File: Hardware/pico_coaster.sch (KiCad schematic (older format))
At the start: 143 parts, among them J1 Conn_02x06_Odd_Even, J2 Conn_02x06_Odd_Even, J3 Conn_02x06_Odd_Even, J4 Conn_01x04, J5 USB_C_Receptacle_USB2.0, SW1 SW_Push, SW2 SW_Push, SW3 SW_Push, SW4 SW_Push, SW5 SW_Push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

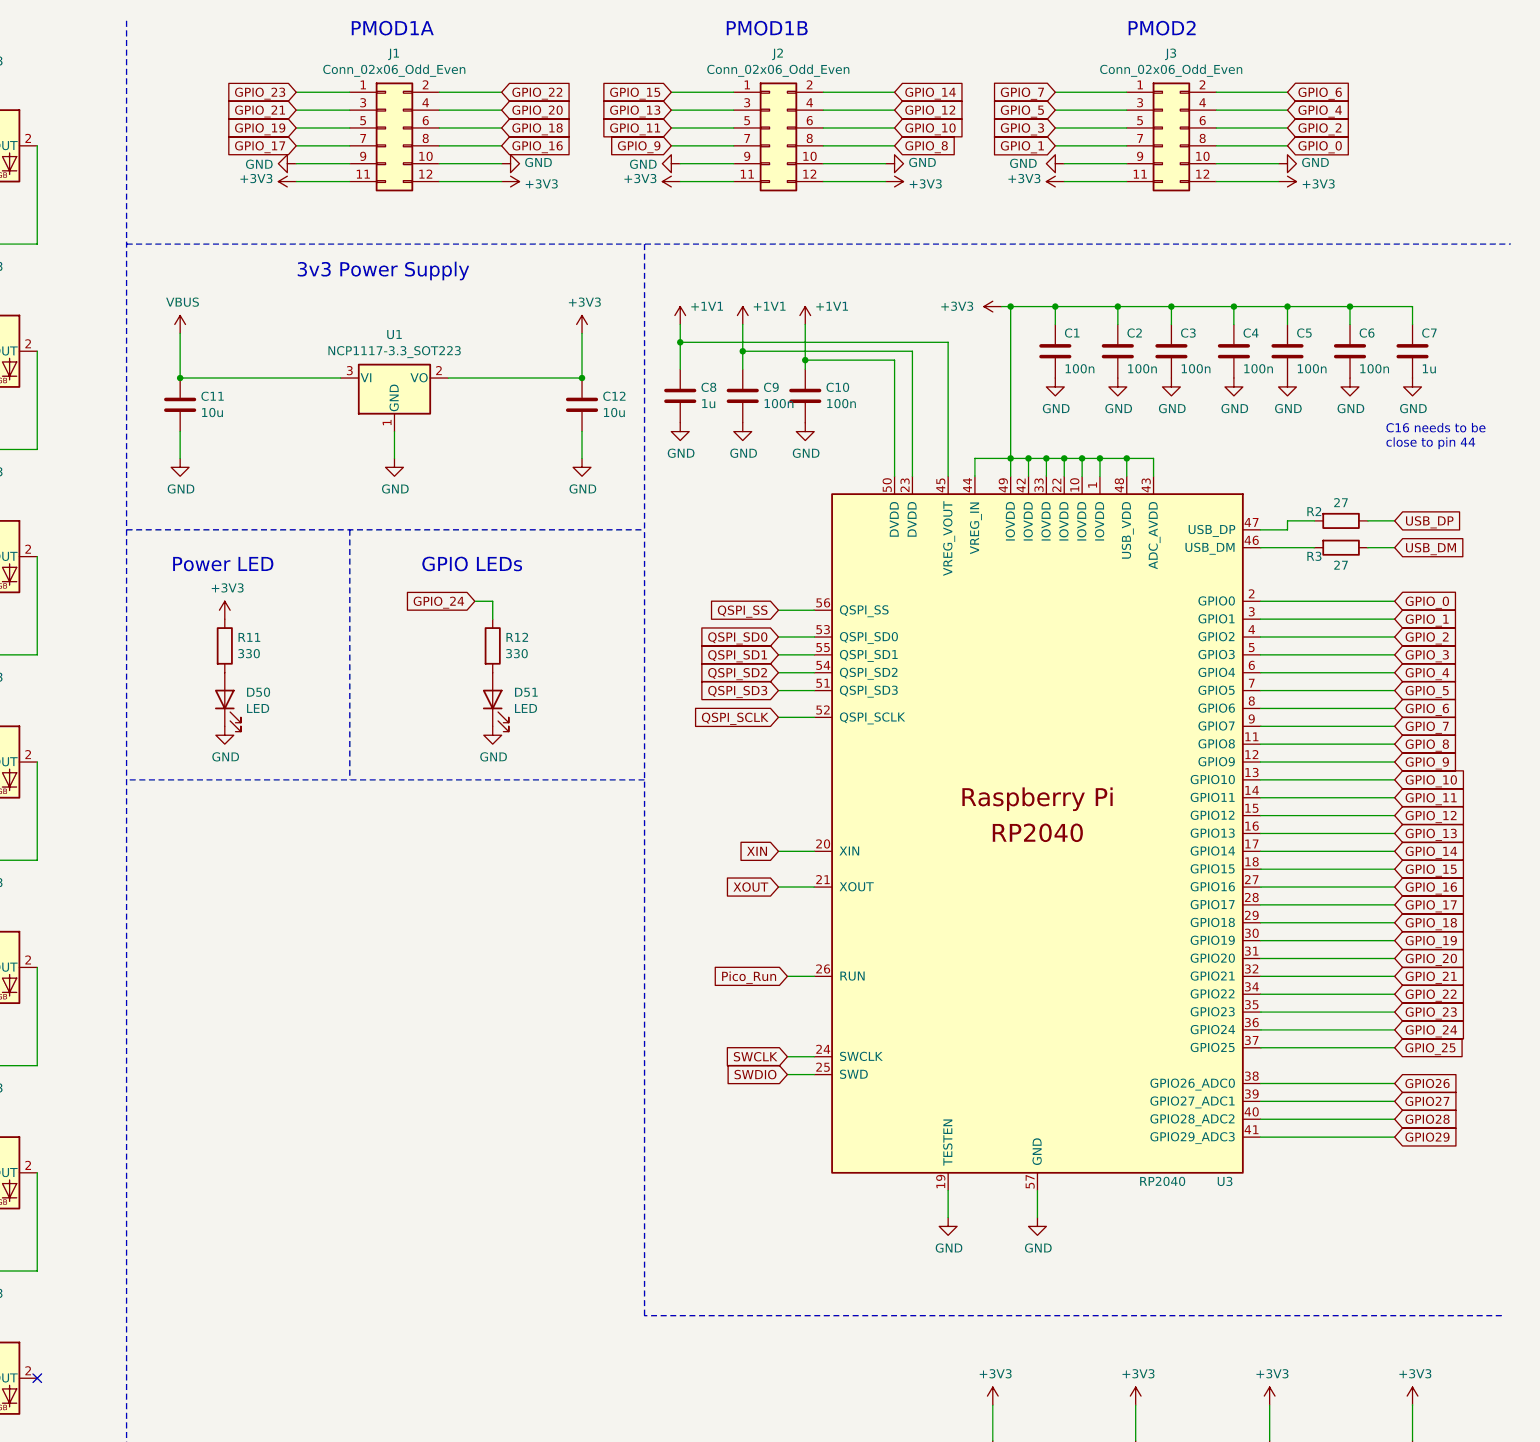
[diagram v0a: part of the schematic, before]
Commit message: reduce Pmod connectors from 3 to 1
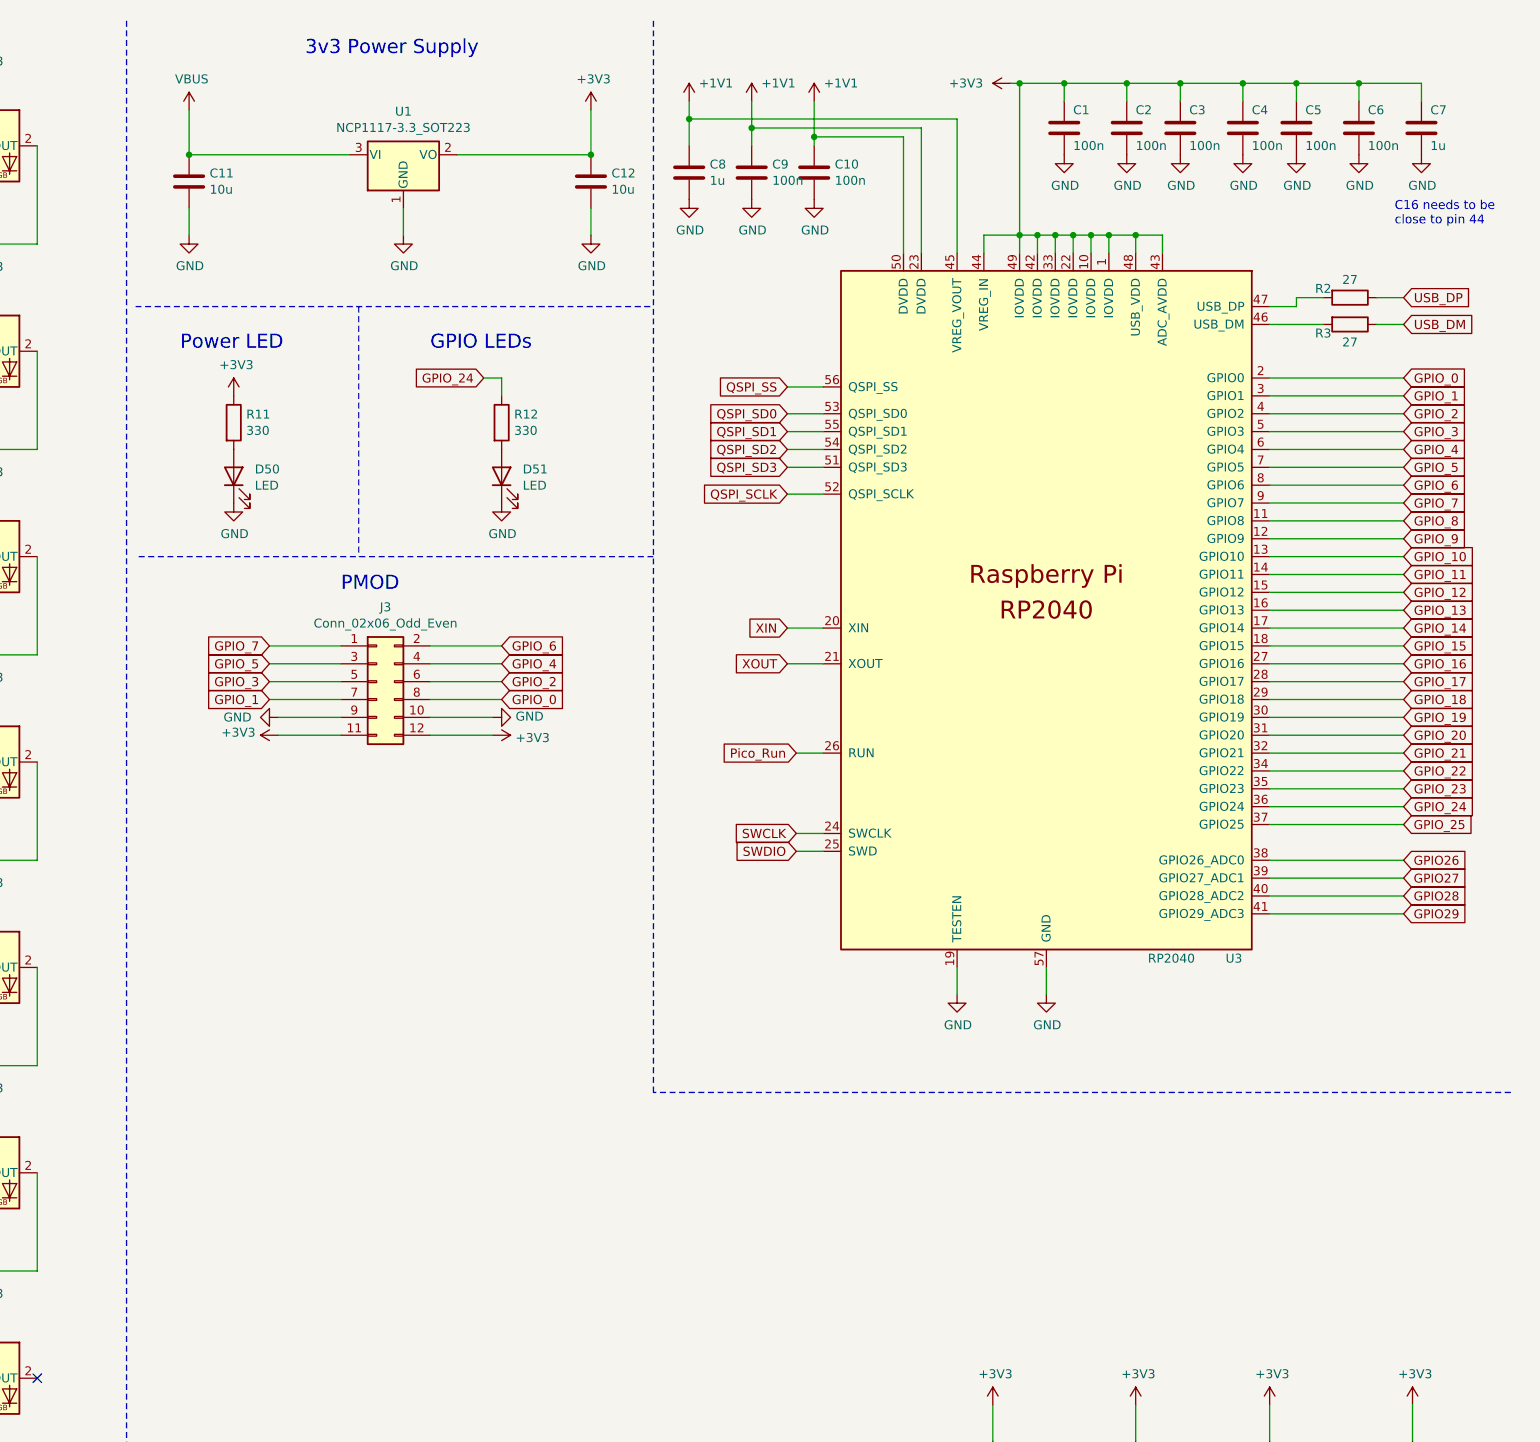
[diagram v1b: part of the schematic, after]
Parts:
- removed J1, J2: Conn_02x06_Odd_Even, Connector_PinHeader_2.54mm:PinHeader_2x06_P2.54mm_Vertical, symbol Connector_Generic:Conn_02x06_Odd_Even
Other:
- note added: "PMOD"
- note removed: "PMOD1A"
- note removed: "PMOD1B"
- note removed: "PMOD2"
- moved on the sheet: C1, C10, C11, C12, C2, C3, C4, C5, C6, C7, C8, C9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

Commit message: Finish layout for the top three LED rows
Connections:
- net GPIO_11: now also R12.1
- net GPIO_24: no longer R12.1
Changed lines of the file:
@@
 $EndComp
 $Comp
-L Device:C C6
-U 1 1 610C63D7
-P 15200 1100
-F 0 "C6" H 15250 1200 50  0000 L CNN
-F 1 "100n" H 15250 1000 50  0000 L CNN
-F 2 "Capacitor_SMD:C_0603_1608Metric" H 15238 950 50  0001 C CNN
-F 3 "~" H 15200 1100 50  0001 C CNN
-	1    15200 1100
-	1    0    0    -1
-$EndComp
-$Comp
 L power:GND #PWR046
 U 1 1 610C63DD
@@
 $EndComp
 Text GLabel 10300 2500 0    50   Input ~ 0
-GPIO_24
+GPIO_11
 Text GLabel 3600 1200 0    50   Input ~ 0
 GPIO_25
@@
 Wire Wire Line
 	14700 5500 15450 5500
+$Comp
+L Device:C C6
+U 1 1 610C63D7
+P 15200 1100
+F 0 "C6" H 15250 1200 50  0000 L CNN
+F 1 "100n" H 15250 1000 50  0000 L CNN
+F 2 "Capacitor_SMD:C_0603_1608Metric" H 15238 950 50  0001 C CNN
+F 3 "~" H 15200 1100 50  0001 C CNN
+	1    15200 1100
+	1    0    0    -1
+$EndComp
 $EndSCHEMATC

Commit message: Swap Boot/Run buttons for pin headers
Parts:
- removed SW1, SW6: SW_Push, Button_Switch_THT:SW_PUSH_6mm_H4.3mm, symbol Switch:SW_Push
- added J1, J2: Conn_01x02, Connector_PinHeader_2.54mm:PinHeader_1x02_P2.54mm_Horizontal, symbol Connector_Generic:Conn_01x02
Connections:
- net GND: now also J1.2 (Pin_2), J2.2 (Pin_2)
- net Pico_Run: now also J1.1 (Pin_1)
- net at R6.2: now also J2.1 (Pin_1)
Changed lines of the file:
@@
 	1    0    0    -1
 $EndComp
-$Comp
-L Switch:SW_Push SW1
-U 1 1 60ECF6F5
-P 1700 8950
-F 0 "SW1" V 1700 9235 50  0000 C CNN
-F 1 "SW_Push" V 1600 9250 50  0000 C CNN
-F 2 "Button_Switch_THT:SW_PUSH_6mm_H4.3mm" H 1700 9150 50  0001 C CNN
-F 3 "~" H 1700 9150 50  0001 C CNN
-	1    1700 8950
-	0    -1   -1   0
-$EndComp
-$Comp
-L Switch:SW_Push SW6
-U 1 1 60ED08D9
-P 1600 10250
-F 0 "SW6" H 1600 10535 50  0000 C CNN
-F 1 "SW_Push" H 1600 10444 50  0000 C CNN
-F 2 "Button_Switch_THT:SW_PUSH_6mm_H4.3mm" H 1600 10450 50  0001 C CNN
-F 3 "~" H 1600 10450 50  0001 C CNN
-	1    1600 10250
-	0    -1   -1   0
-$EndComp
 Text Notes 1600 9500 0    79   ~ 0
 Pico Run
@@
 Wire Wire Line
 	1700 8150 1700 8300
-Wire Wire Line
-	1700 8600 1700 8750
 Text GLabel 1850 9800 2    51   Input ~ 0
 Pico_Run
@@
 $EndComp
 Wire Wire Line
-	1600 10650 1600 10450
-Wire Wire Line
-	1600 10050 1600 9800
-Wire Wire Line
 	1600 9800 1850 9800
 $Comp
@@
 	1    0    0    -1
 $EndComp
+$Comp
+L Connector_Generic:Conn_01x02 J2
+U 1 1 61DB34E0
+P 1900 8850
+F 0 "J2" H 1980 8842 50  0000 L CNN
+F 1 "Conn_01x02" H 1980 8751 50  0000 L CNN
+F 2 "Connector_PinHeader_2.54mm:PinHeader_1x02_P2.54mm_Horizontal" H 1900 8850 50  0001 C CNN
+F 3 "~" H 1900 8850 50  0001 C CNN
+	1    1900 8850
+	1    0    0    -1
+$EndComp
+$Comp
+L Connector_Generic:Conn_01x02 J1
+U 1 1 61DB94D2
+P 1800 10200
+F 0 "J1" H 1880 10192 50  0000 L CNN
+F 1 "Conn_01x02" H 1880 10101 50  0000 L CNN
+F 2 "Connector_PinHeader_2.54mm:PinHeader_1x02_P2.54mm_Horizontal" H 1800 10200 50  0001 C CNN
+F 3 "~" H 1800 10200 50  0001 C CNN
+	1    1800 10200
+	1    0    0    -1
+$EndComp
+Wire Wire Line
+	1700 8600 1700 8850
+Wire Wire Line
+	1700 8950 1700 9150
+Wire Wire Line
+	1600 9800 1600 10200
+Wire Wire Line
+	1600 10300 1600 10650
 $EndSCHEMATC

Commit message: Fix DRC errors
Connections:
- net GPIO_10: no longer names the net of U3.13 (GPIO10)
- net GPIO_12: no longer names the net of U3.15 (GPIO12)
- net GPIO_13: no longer names the net of U3.16 (GPIO13)
- net GPIO_14: no longer names the net of U3.17 (GPIO14)
- net GPIO_15: no longer names the net of U3.18 (GPIO15)
- net GPIO_16: no longer names the net of U3.27 (GPIO16)
- net GPIO_17: no longer names the net of U3.28 (GPIO17)
- net GPIO_18: no longer names the net of U3.29 (GPIO18)
- net GPIO_19: no longer names the net of U3.30 (GPIO19)
- net GPIO_20: no longer names the net of U3.31 (GPIO20)
- net GPIO_21: no longer names the net of U3.32 (GPIO21)
- net GPIO_22: no longer names the net of U3.34 (GPIO22)
- net GPIO_23: no longer names the net of U3.35 (GPIO23)
- net GPIO_24: no longer names the net of U3.36 (GPIO24)
- net GPIO_8: no longer names the net of U3.11 (GPIO8)
- net GPIO_9: no longer names the net of U3.12 (GPIO9)
- no-connect marks 3 -> 20
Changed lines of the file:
@@
 Text GLabel 15450 3200 2    51   Input ~ 0
 GPIO_7
-Text GLabel 15450 3300 2    51   Input ~ 0
-GPIO_8
-Text GLabel 15450 3400 2    51   Input ~ 0
-GPIO_9
-Text GLabel 15450 3500 2    51   Input ~ 0
-GPIO_10
 Text GLabel 15450 3600 2    51   Input ~ 0
 GPIO_11
-Text GLabel 15450 3700 2    51   Input ~ 0
-GPIO_12
-Text GLabel 15450 3800 2    51   Input ~ 0
-GPIO_13
-Text GLabel 15450 4000 2    51   Input ~ 0
-GPIO_15
-Text GLabel 15450 3900 2    51   Input ~ 0
-GPIO_14
-Text GLabel 15450 4100 2    51   Input ~ 0
-GPIO_16
-Text GLabel 15450 4200 2    51   Input ~ 0
-GPIO_17
-Text GLabel 15450 4300 2    51   Input ~ 0
-GPIO_18
-Text GLabel 15450 4400 2    51   Input ~ 0
-GPIO_19
-Text GLabel 15450 4500 2    51   Input ~ 0
-GPIO_20
-Text GLabel 15450 4600 2    51   Input ~ 0
-GPIO_21
-Text GLabel 15450 4700 2    51   Input ~ 0
-GPIO_22
-Text GLabel 15450 4800 2    51   Input ~ 0
-GPIO_23
-Text GLabel 15450 4900 2    51   Input ~ 0
-GPIO_24
 Wire Wire Line
 	14700 2900 15450 2900
@@
 Wire Wire Line
 	10400 2500 10300 2500
-Text GLabel 15450 5000 2    50   Input ~ 0
-GPIO_25
 Wire Wire Line
 	15450 5000 14700 5000
@@
 Wire Notes Line
 	9600 2100 9600 3500
-Text GLabel 15450 5200 2    50   Input ~ 0
-GPIO26
-Text GLabel 15450 5300 2    50   Input ~ 0
-GPIO27
-Text GLabel 15450 5400 2    50   Input ~ 0
-GPIO28
-Text GLabel 15450 5500 2    50   Input ~ 0
-GPIO29
 Wire Wire Line
 	15450 5200 14700 5200
@@
 Wire Wire Line
 	1600 10300 1600 10650
+NoConn ~ 15450 3300
+NoConn ~ 15450 3400
+NoConn ~ 15450 3500
+NoConn ~ 15450 3700
+NoConn ~ 15450 3800
+NoConn ~ 15450 3900
+NoConn ~ 15450 4000
+NoConn ~ 15450 4100
+NoConn ~ 15450 4200
+NoConn ~ 15450 4300
+NoConn ~ 15450 4400
+NoConn ~ 15450 4500
+NoConn ~ 15450 4600
+NoConn ~ 15450 4700
+NoConn ~ 15450 4800
+NoConn ~ 15450 4900
+NoConn ~ 15850 3350
+Text GLabel 15450 5200 2    51   Input ~ 0
+GPIO26
+Text GLabel 15450 5300 2    51   Input ~ 0
+GPIO27
+Text GLabel 15450 5400 2    51   Input ~ 0
+GPIO28
+Text GLabel 15450 5500 2    51   Input ~ 0
+GPIO29
+Text GLabel 15450 5000 2    51   Input ~ 0
+GPIO_25
 $EndSCHEMATC

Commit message: Add 2.54mm power in connector
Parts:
- added J?: Conn_01x02, Connector_PinHeader_2.54mm:PinHeader_1x02_P2.54mm_Horizontal, symbol Connector_Generic:Conn_01x02
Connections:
- net GND: now also J?.2 (Pin_2)
- net VBUS: now also J?.1 (Pin_1)
- no-connect marks 20 -> 19
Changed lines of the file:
@@
 Text GLabel 15450 3200 2    51   Input ~ 0
 GPIO_7
-Text GLabel 15450 3600 2    51   Input ~ 0
-GPIO_11
 Wire Wire Line
 	14700 2900 15450 2900
@@
 NoConn ~ 15450 4800
 NoConn ~ 15450 4900
-NoConn ~ 15850 3350
 Text GLabel 15450 5200 2    51   Input ~ 0
 GPIO26
@@
 Text GLabel 15450 5000 2    51   Input ~ 0
 GPIO_25
+Text GLabel 15450 3600 2    51   Input ~ 0
+GPIO_11
+$Comp
+L power:GND #PWR?
+U 1 1 62410365
+P 8750 9600
+F 0 "#PWR?" H 8750 9350 50  0001 C CNN
+F 1 "GND" H 8600 9500 50  0000 C CNN
+F 2 "" H 8750 9600 50  0001 C CNN
+F 3 "" H 8750 9600 50  0001 C CNN
+	1    8750 9600
+	1    0    0    -1
+$EndComp
+$Comp
+L Connector_Generic:Conn_01x02 J?
+U 1 1 6241036B
+P 8950 9150
+F 0 "J?" H 9030 9142 50  0000 L CNN
+F 1 "Conn_01x02" H 9030 9051 50  0000 L CNN
+F 2 "Connector_PinHeader_2.54mm:PinHeader_1x02_P2.54mm_Horizontal" H 8950 9150 50  0001 C CNN
+F 3 "~" H 8950 9150 50  0001 C CNN
+	1    8950 9150
+	1    0    0    -1
+$EndComp
+Wire Wire Line
+	8750 8750 8750 9150
+Wire Wire Line
+	8750 9250 8750 9600
+$Comp
+L power:VBUS #PWR?
+U 1 1 624447BD
+P 8750 8750
+F 0 "#PWR?" H 8750 8600 50  0001 C CNN
+F 1 "VBUS" H 8765 8923 50  0000 C CNN
+F 2 "" H 8750 8750 50  0001 C CNN
+F 3 "" H 8750 8750 50  0001 C CNN
+	1    8750 8750
+	1    0    0    -1
+$EndComp
 $EndSCHEMATC

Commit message: update chematic with number
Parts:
- gave numbers to parts that had none: 1
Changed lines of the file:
@@
 GPIO_11
 $Comp
-L power:GND #PWR?
+L power:GND #PWR0168
 U 1 1 62410365
 P 8750 9600
-F 0 "#PWR?" H 8750 9350 50  0001 C CNN
+F 0 "#PWR0168" H 8750 9350 50  0001 C CNN
 F 1 "GND" H 8600 9500 50  0000 C CNN
 F 2 "" H 8750 9600 50  0001 C CNN
@@
 $EndComp
 $Comp
-L Connector_Generic:Conn_01x02 J?
+L Connector_Generic:Conn_01x02 J6
 U 1 1 6241036B
 P 8950 9150
-F 0 "J?" H 9030 9142 50  0000 L CNN
+F 0 "J6" H 9030 9142 50  0000 L CNN
 F 1 "Conn_01x02" H 9030 9051 50  0000 L CNN
 F 2 "Connector_PinHeader_2.54mm:PinHeader_1x02_P2.54mm_Horizontal" H 8950 9150 50  0001 C CNN
@@
 	8750 9250 8750 9600
 $Comp
-L power:VBUS #PWR?
+L power:VBUS #PWR0169
 U 1 1 624447BD
 P 8750 8750
-F 0 "#PWR?" H 8750 8600 50  0001 C CNN
+F 0 "#PWR0169" H 8750 8600 50  0001 C CNN
 F 1 "VBUS" H 8765 8923 50  0000 C CNN
 F 2 "" H 8750 8750 50  0001 C CNN

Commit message: change clk capasitors
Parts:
- C13, C14: value 20p -> 10p
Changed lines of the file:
@@
 P 1300 3250
 F 0 "C13" H 1000 3300 50  0000 L CNN
-F 1 "20p" H 1000 3200 50  0000 L CNN
+F 1 "10p" H 1000 3200 50  0000 L CNN
 F 2 "Capacitor_SMD:C_0603_1608Metric" H 1338 3100 50  0001 C CNN
 F 3 "~" H 1300 3250 50  0001 C CNN
@@
 P 2100 3250
 F 0 "C14" H 2215 3296 50  0000 L CNN
-F 1 "20p" H 2215 3205 50  0000 L CNN
+F 1 "10p" H 2215 3205 50  0000 L CNN
 F 2 "Capacitor_SMD:C_0603_1608Metric" H 2138 3100 50  0001 C CNN
 F 3 "~" H 2100 3250 50  0001 C CNN
